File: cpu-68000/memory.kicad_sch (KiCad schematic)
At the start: 16 parts, among them U401 SST39SF040-55-4C, U402 SST39SF040-55-4C, U403 IS61C5128AL-10TLI, U404 IS61C5128AL-10TLI

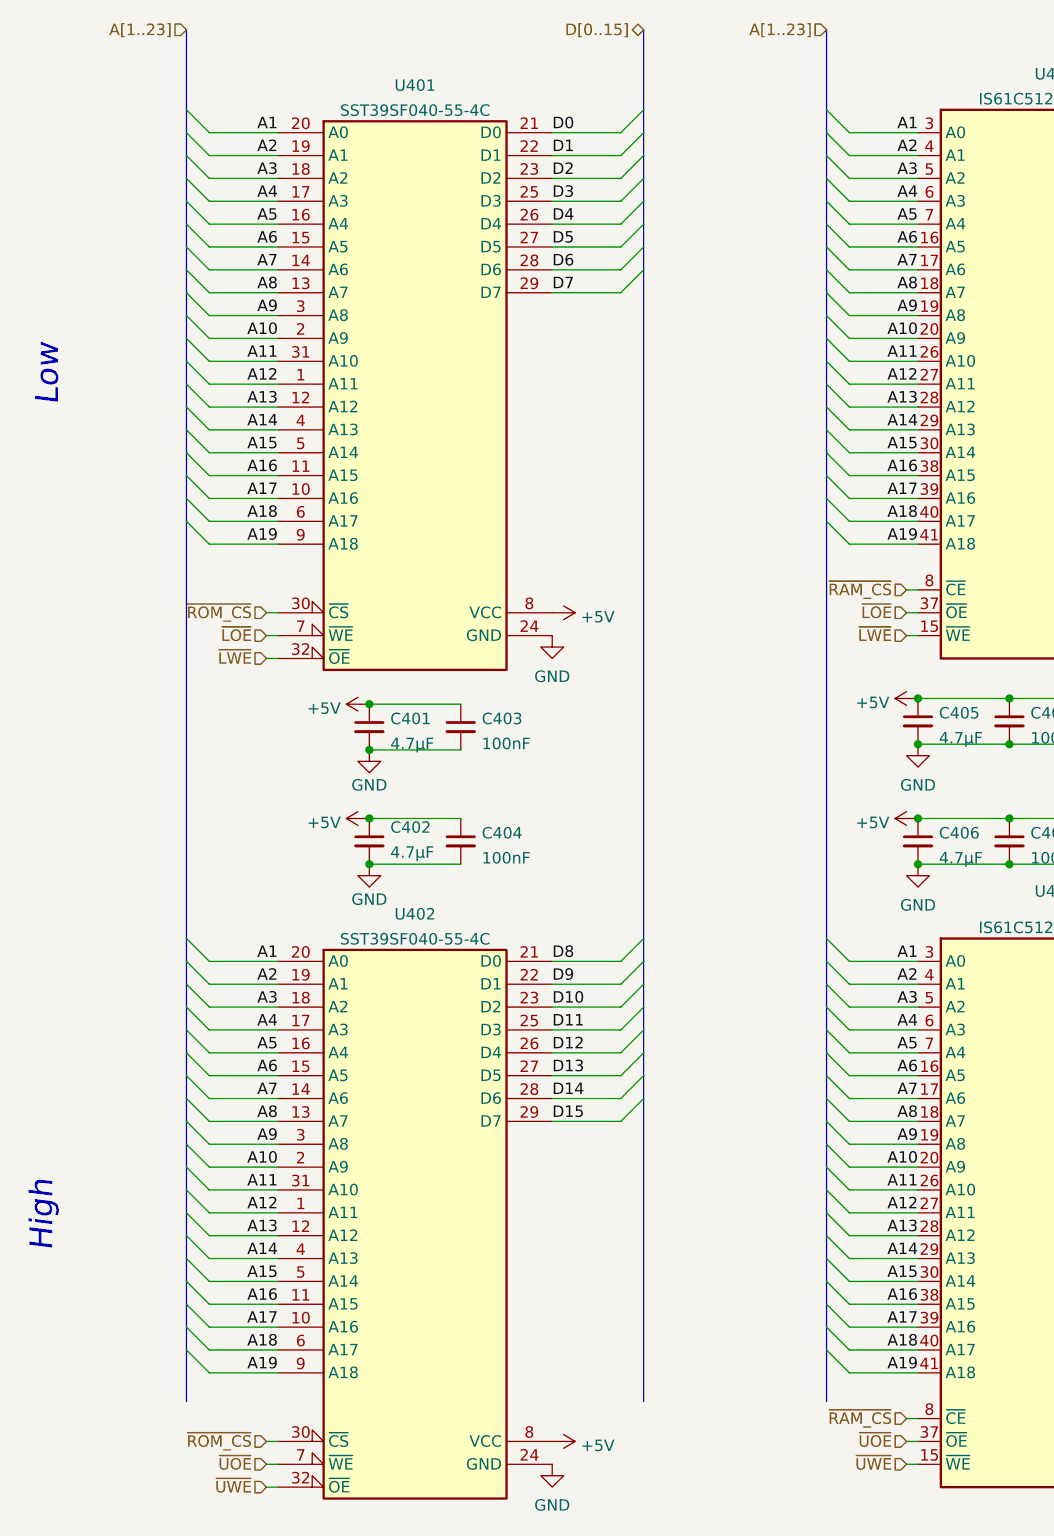
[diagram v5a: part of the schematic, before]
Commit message: Begin routing stuff
- Routed most control signals to GALs, finished routing signals to bus
  transceivers (except data bus)

- Removed ROMs but doubled up RAM; the boot ROM will be provided by an
  external board

- Added dual SAA1099 chips (audio out via backplane)

- Pullups on some external irq/bus request lines
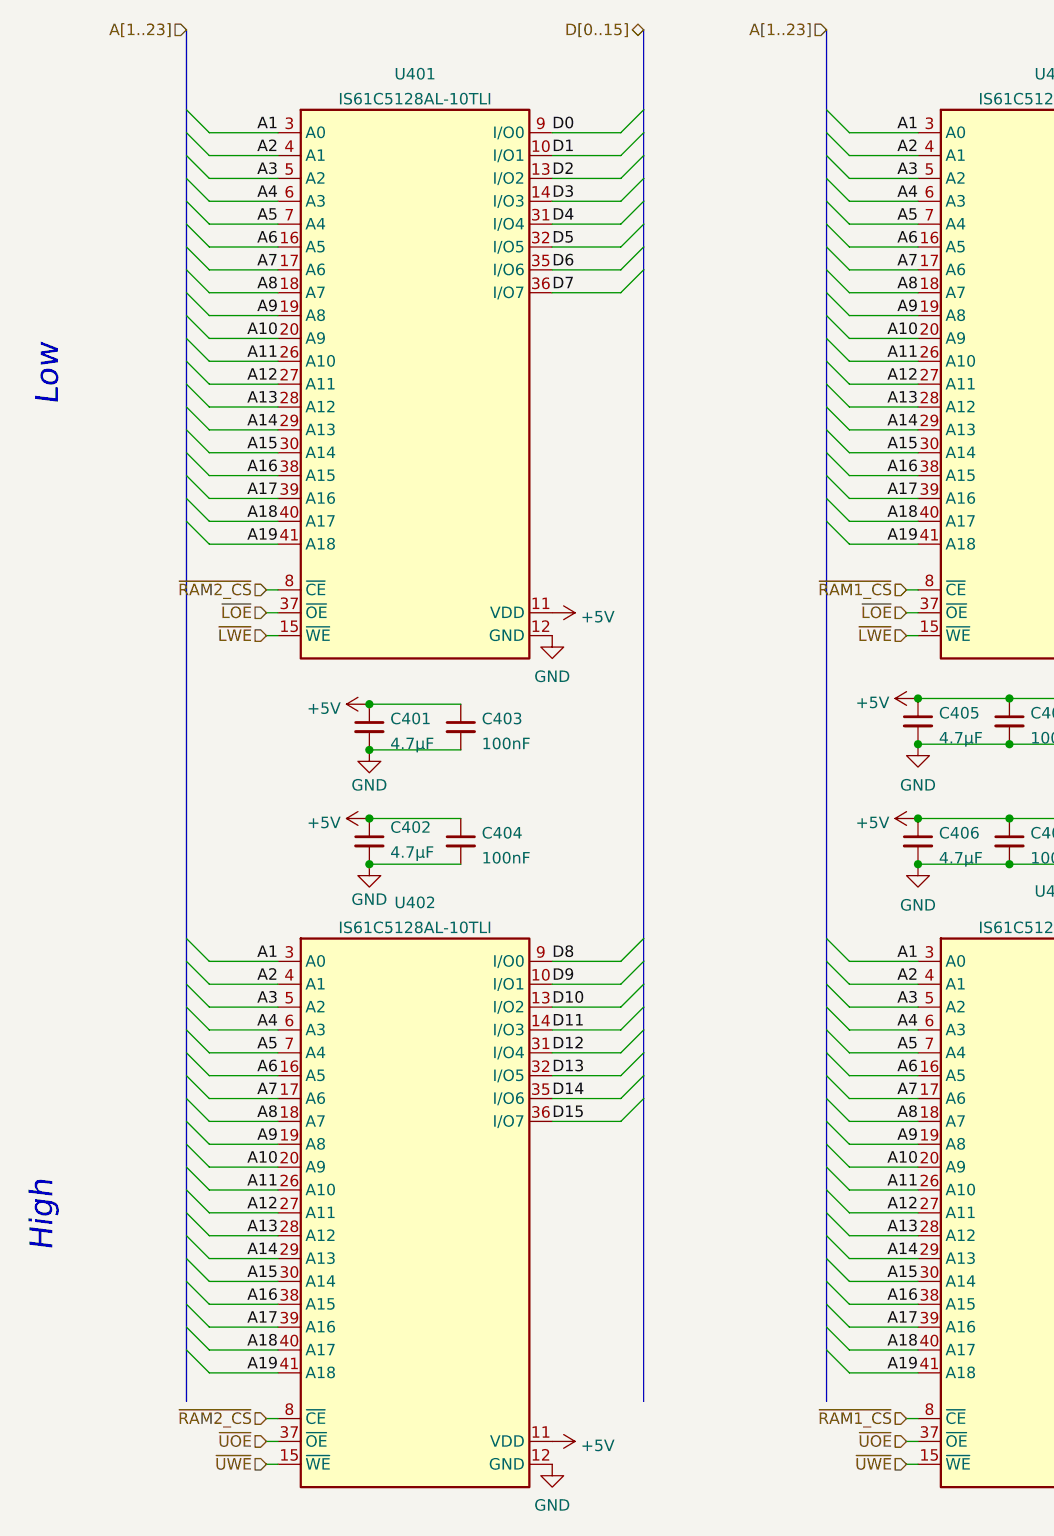
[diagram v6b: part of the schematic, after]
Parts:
- removed U401, U402: SST39SF040-55-4C, Package_SO:TSOP-I-32_11.8x8mm_P0.5mm, symbol 68komputer-common:SST39SF040-XX-4X-W
- added U401, U402: IS61C5128AL-10TLI, Package_SO:TSOP-II-44_10.16x18.41mm_P0.8mm, symbol 68komputer-common:IS61C5128AL-10TLI
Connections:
- net +5V: now also U401.11 (VDD), U401.33 (VDD), U402.11 (VDD), U402.33 (VDD)
- net A1: now also U401.3 (A0), U402.3 (A0)
- net A10: now also U401.20 (A9), U402.20 (A9)
- net A11: now also U401.26 (A10), U402.26 (A10)
- net A12: now also U401.27 (A11), U402.27 (A11)
- net A13: now also U401.28 (A12), U402.28 (A12)
- net A14: now also U401.29 (A13), U402.29 (A13)
- net A15: now also U401.30 (A14), U402.30 (A14)
- net A16: now also U401.38 (A15), U402.38 (A15)
- net A17: now also U401.39 (A16), U402.39 (A16)
- net A18: now also U401.40 (A17), U402.40 (A17)
- net A19: now also U401.41 (A18), U402.41 (A18)
- net A2: now also U401.4 (A1), U402.4 (A1)
- net A3: now also U401.5 (A2), U402.5 (A2)
- net A4: now also U401.6 (A3), U402.6 (A3)
- net A5: now also U401.7 (A4), U402.7 (A4)
- net A6: now also U401.16 (A5), U402.16 (A5)
- net A7: now also U401.17 (A6), U402.17 (A6)
- net A8: now also U401.18 (A7), U402.18 (A7)
- net A9: now also U401.19 (A8), U402.19 (A8)
- net D0: now also U401.9 (I/O0)
- net D1: now also U401.10 (I/O1)
- net D10: now also U402.13 (I/O2)
- net D11: now also U402.14 (I/O3)
- net D12: now also U402.31 (I/O4)
- net D13: now also U402.32 (I/O5)
- net D14: now also U402.35 (I/O6)
- net D15: now also U402.36 (I/O7)
- net D2: now also U401.13 (I/O2)
- net D3: now also U401.14 (I/O3)
- net D4: now also U401.31 (I/O4)
- net D5: now also U401.32 (I/O5)
- net D6: now also U401.35 (I/O6)
- net D7: now also U401.36 (I/O7)
- net D8: now also U402.9 (I/O0)
- net D9: now also U402.10 (I/O1)
- net GND: now also U401.12 (GND), U401.34 (GND), U402.12 (GND), U402.34 (GND)
- net ~{LOE}: now also U401.37 (~{OE})
- net ~{LWE}: now also U401.15 (~{WE})
- net ~{UOE}: now also U402.37 (~{OE})
- net ~{UWE}: now also U402.15 (~{WE})
- net ~{RAM_CS} renamed ~{RAM1_CS}
- new net ~{RAM2_CS}: U401.8 (~{CE}), U402.8 (~{CE})

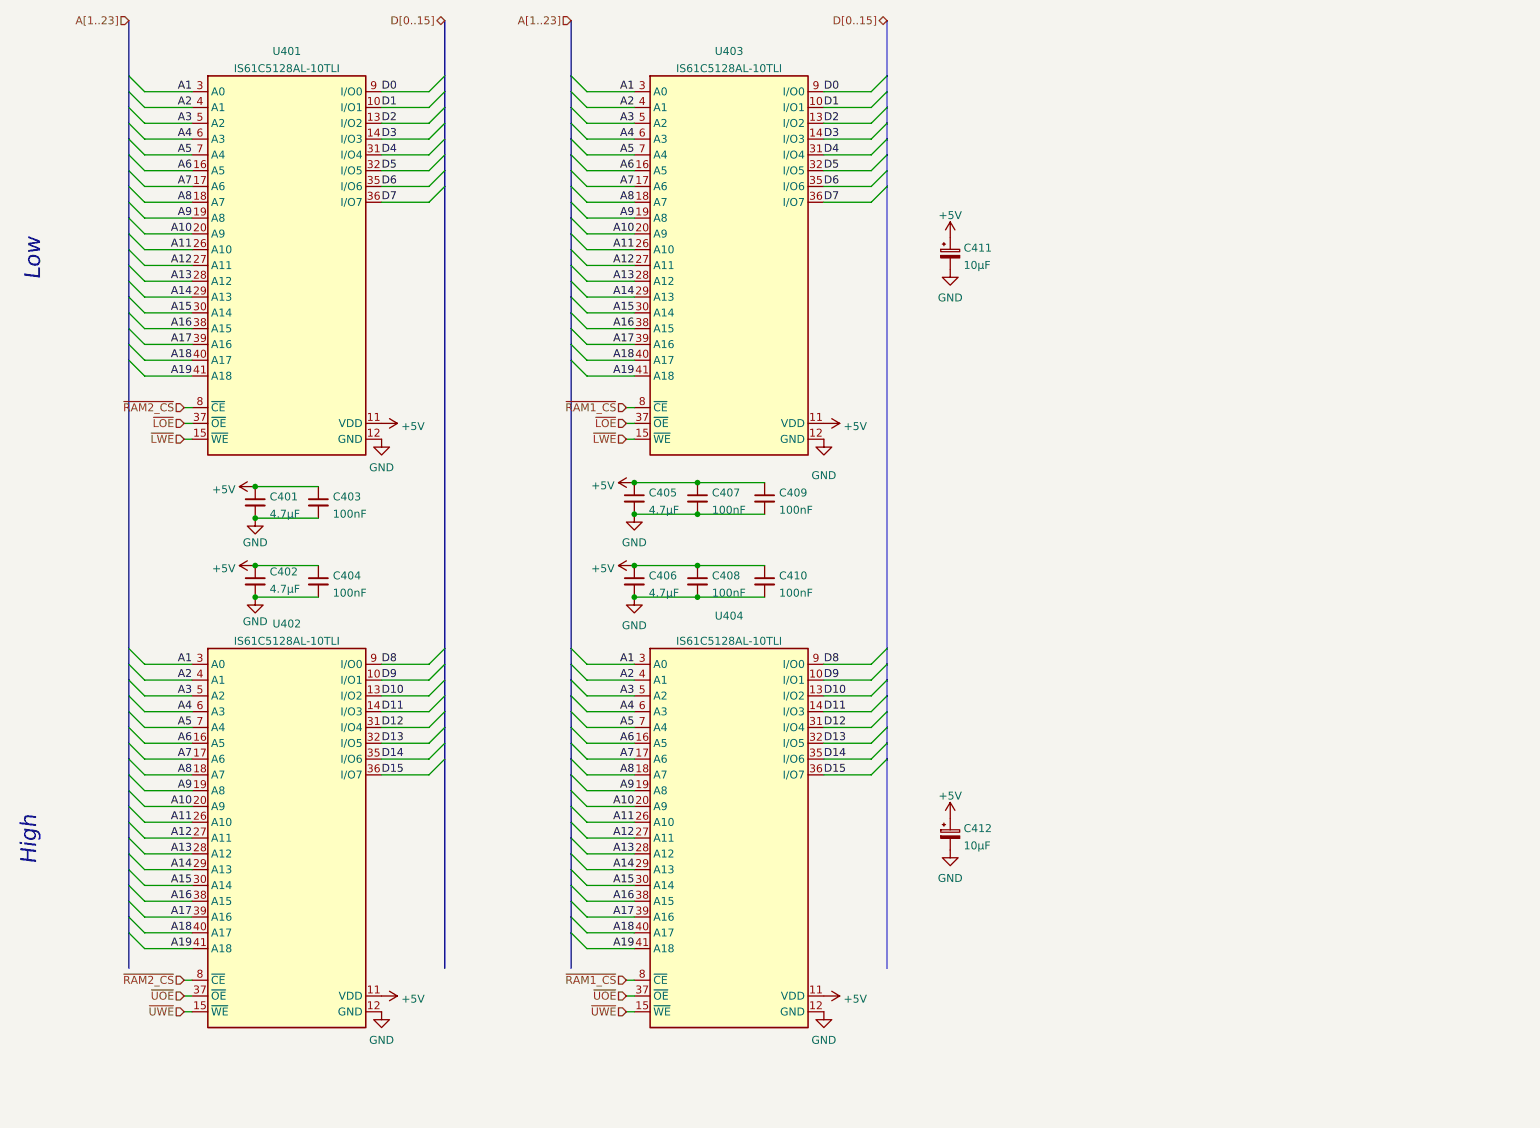
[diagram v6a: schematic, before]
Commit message: Mostly completed RAM routing
- Finished routing the address and data busses for RAMs; connected the
  address bus to the 68k, the high byte of data bus is connected but not
  yet low.

- Connected more control signals to GALs

- Finished connecting data bus to bus transceivers

- Fixed clearance setting for traces (matching JLCPCB impedance
  controlled 4 layer stackup)
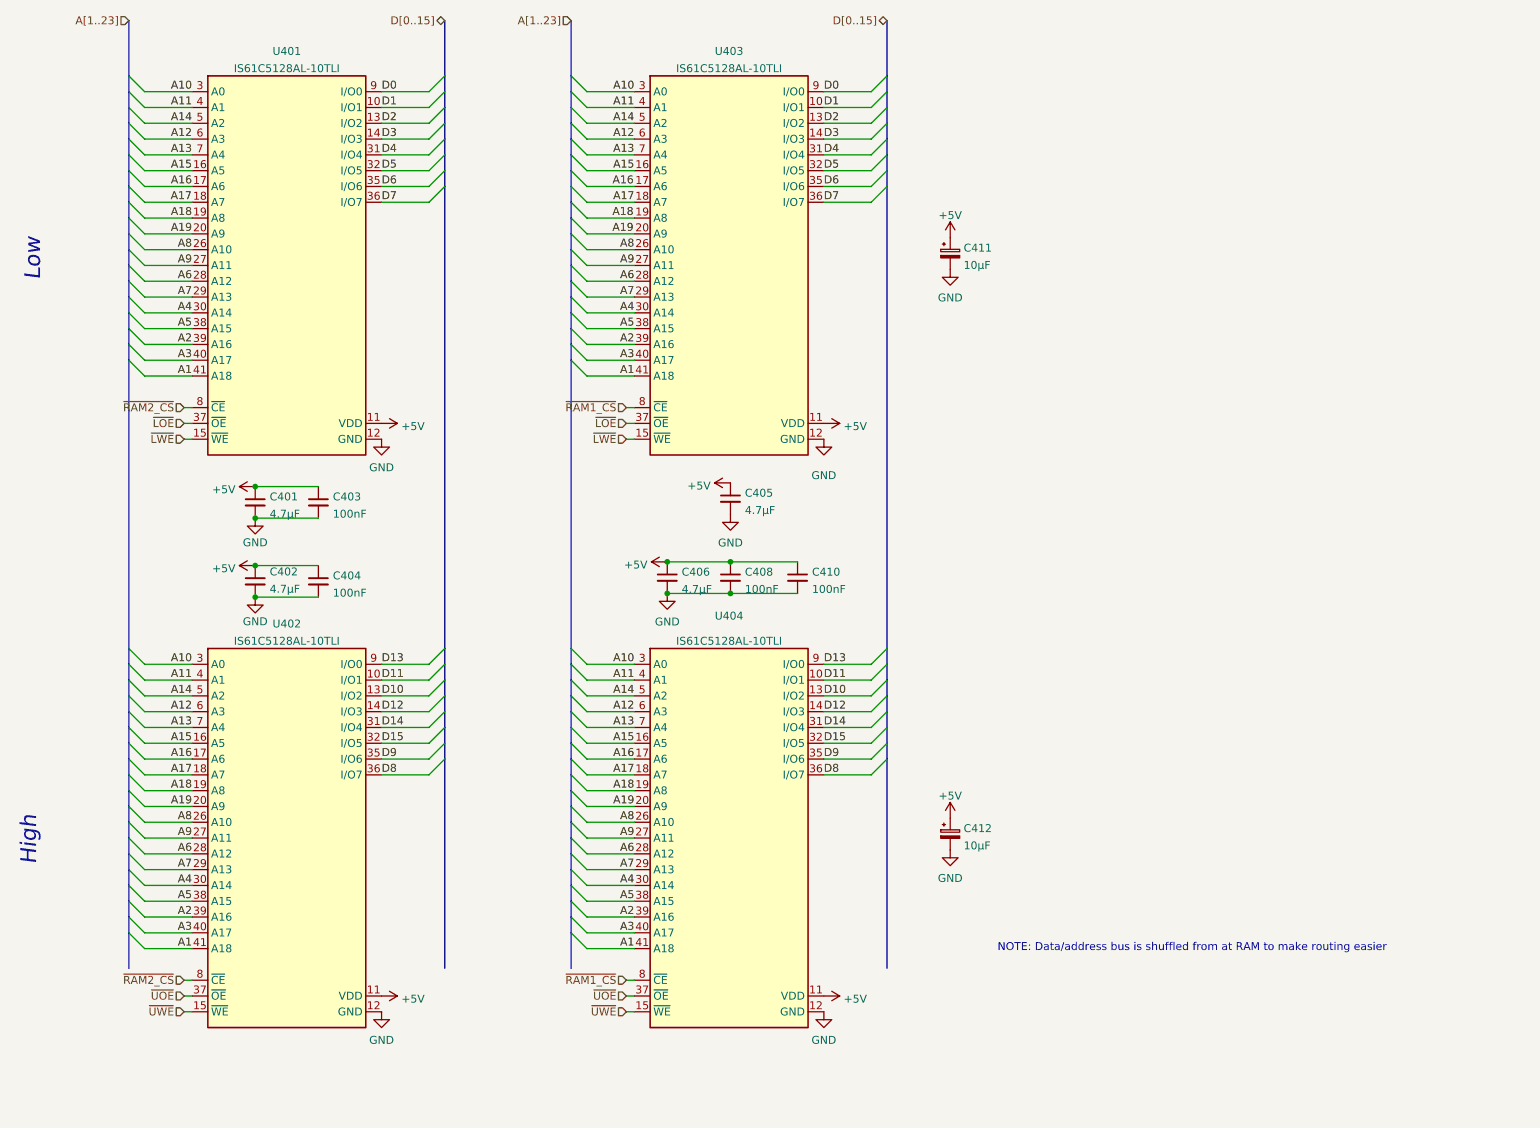
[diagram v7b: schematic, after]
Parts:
- removed C407, C409: 100nF, Capacitor_SMD:C_0805_2012Metric, symbol Device:C_Small
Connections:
- net A1: now also U401.41 (A18), U402.41 (A18), U403.41 (A18), U404.41 (A18); no longer U401.3 (A0), U402.3 (A0), U403.3 (A0), U404.3 (A0)
- net A10: now also U401.3 (A0), U402.3 (A0), U403.3 (A0), U404.3 (A0); no longer U401.20 (A9), U402.20 (A9), U403.20 (A9), U404.20 (A9)
- net A11: now also U401.4 (A1), U402.4 (A1), U403.4 (A1), U404.4 (A1); no longer U401.26 (A10), U402.26 (A10), U403.26 (A10), U404.26 (A10)
- net A12: now also U401.6 (A3), U402.6 (A3), U403.6 (A3), U404.6 (A3); no longer U401.27 (A11), U402.27 (A11), U403.27 (A11), U404.27 (A11)
- net A13: now also U401.7 (A4), U402.7 (A4), U403.7 (A4), U404.7 (A4); no longer U401.28 (A12), U402.28 (A12), U403.28 (A12), U404.28 (A12)
- net A14: now also U401.5 (A2), U402.5 (A2), U403.5 (A2), U404.5 (A2); no longer U401.29 (A13), U402.29 (A13), U403.29 (A13), U404.29 (A13)
- net A15: now also U401.16 (A5), U402.16 (A5), U403.16 (A5), U404.16 (A5); no longer U401.30 (A14), U402.30 (A14), U403.30 (A14), U404.30 (A14)
- net A16: now also U401.17 (A6), U402.17 (A6), U403.17 (A6), U404.17 (A6); no longer U401.38 (A15), U402.38 (A15), U403.38 (A15), U404.38 (A15)
- net A17: now also U401.18 (A7), U402.18 (A7), U403.18 (A7), U404.18 (A7); no longer U401.39 (A16), U402.39 (A16), U403.39 (A16), U404.39 (A16)
- net A18: now also U401.19 (A8), U402.19 (A8), U403.19 (A8), U404.19 (A8); no longer U401.40 (A17), U402.40 (A17), U403.40 (A17), U404.40 (A17)
- net A19: now also U401.20 (A9), U402.20 (A9), U403.20 (A9), U404.20 (A9); no longer U401.41 (A18), U402.41 (A18), U403.41 (A18), U404.41 (A18)
- net A2: now also U401.39 (A16), U402.39 (A16), U403.39 (A16), U404.39 (A16); no longer U401.4 (A1), U402.4 (A1), U403.4 (A1), U404.4 (A1)
- net A3: now also U401.40 (A17), U402.40 (A17), U403.40 (A17), U404.40 (A17); no longer U401.5 (A2), U402.5 (A2), U403.5 (A2), U404.5 (A2)
- net A4: now also U401.30 (A14), U402.30 (A14), U403.30 (A14), U404.30 (A14); no longer U401.6 (A3), U402.6 (A3), U403.6 (A3), U404.6 (A3)
- net A5: now also U401.38 (A15), U402.38 (A15), U403.38 (A15), U404.38 (A15); no longer U401.7 (A4), U402.7 (A4), U403.7 (A4), U404.7 (A4)
- net A6: now also U401.28 (A12), U402.28 (A12), U403.28 (A12), U404.28 (A12); no longer U401.16 (A5), U402.16 (A5), U403.16 (A5), U404.16 (A5)
- net A7: now also U401.29 (A13), U402.29 (A13), U403.29 (A13), U404.29 (A13); no longer U401.17 (A6), U402.17 (A6), U403.17 (A6), U404.17 (A6)
- net A8: now also U401.26 (A10), U402.26 (A10), U403.26 (A10), U404.26 (A10); no longer U401.18 (A7), U402.18 (A7), U403.18 (A7), U404.18 (A7)
- net A9: now also U401.27 (A11), U402.27 (A11), U403.27 (A11), U404.27 (A11); no longer U401.19 (A8), U402.19 (A8), U403.19 (A8), U404.19 (A8)
- net D11: now also U402.10 (I/O1), U404.10 (I/O1); no longer U402.14 (I/O3), U404.14 (I/O3)
- net D12: now also U402.14 (I/O3), U404.14 (I/O3); no longer U402.31 (I/O4), U404.31 (I/O4)
- net D13: now also U402.9 (I/O0), U404.9 (I/O0); no longer U402.32 (I/O5), U404.32 (I/O5)
- net D14: now also U402.31 (I/O4), U404.31 (I/O4); no longer U402.35 (I/O6), U404.35 (I/O6)
- net D15: now also U402.32 (I/O5), U404.32 (I/O5); no longer U402.36 (I/O7), U404.36 (I/O7)
- net D8: now also U402.36 (I/O7), U404.36 (I/O7); no longer U402.9 (I/O0), U404.9 (I/O0)
- net D9: now also U402.35 (I/O6), U404.35 (I/O6); no longer U402.10 (I/O1), U404.10 (I/O1)
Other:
- note added: "NOTE: Data/address bus is shuffled from at RAM to make routing easier"
- moved on the sheet: C405, C406, C408, C410
